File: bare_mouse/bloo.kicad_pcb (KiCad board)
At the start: 2 copper layers, 100 x 100 mm, 103 parts, among them J1 Serial Debug Header, J10 Conn_01x06_Female, J2 SWD Header, J4 Conn_ARM_JTAG_SWD_10, J5 SWD Header, M1 M1_Conn_Alt, M2 M2_Conn_Alt, Q0 TEFT4300, Q1 TEFT4300, Q10 Q_NMOS_GSD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

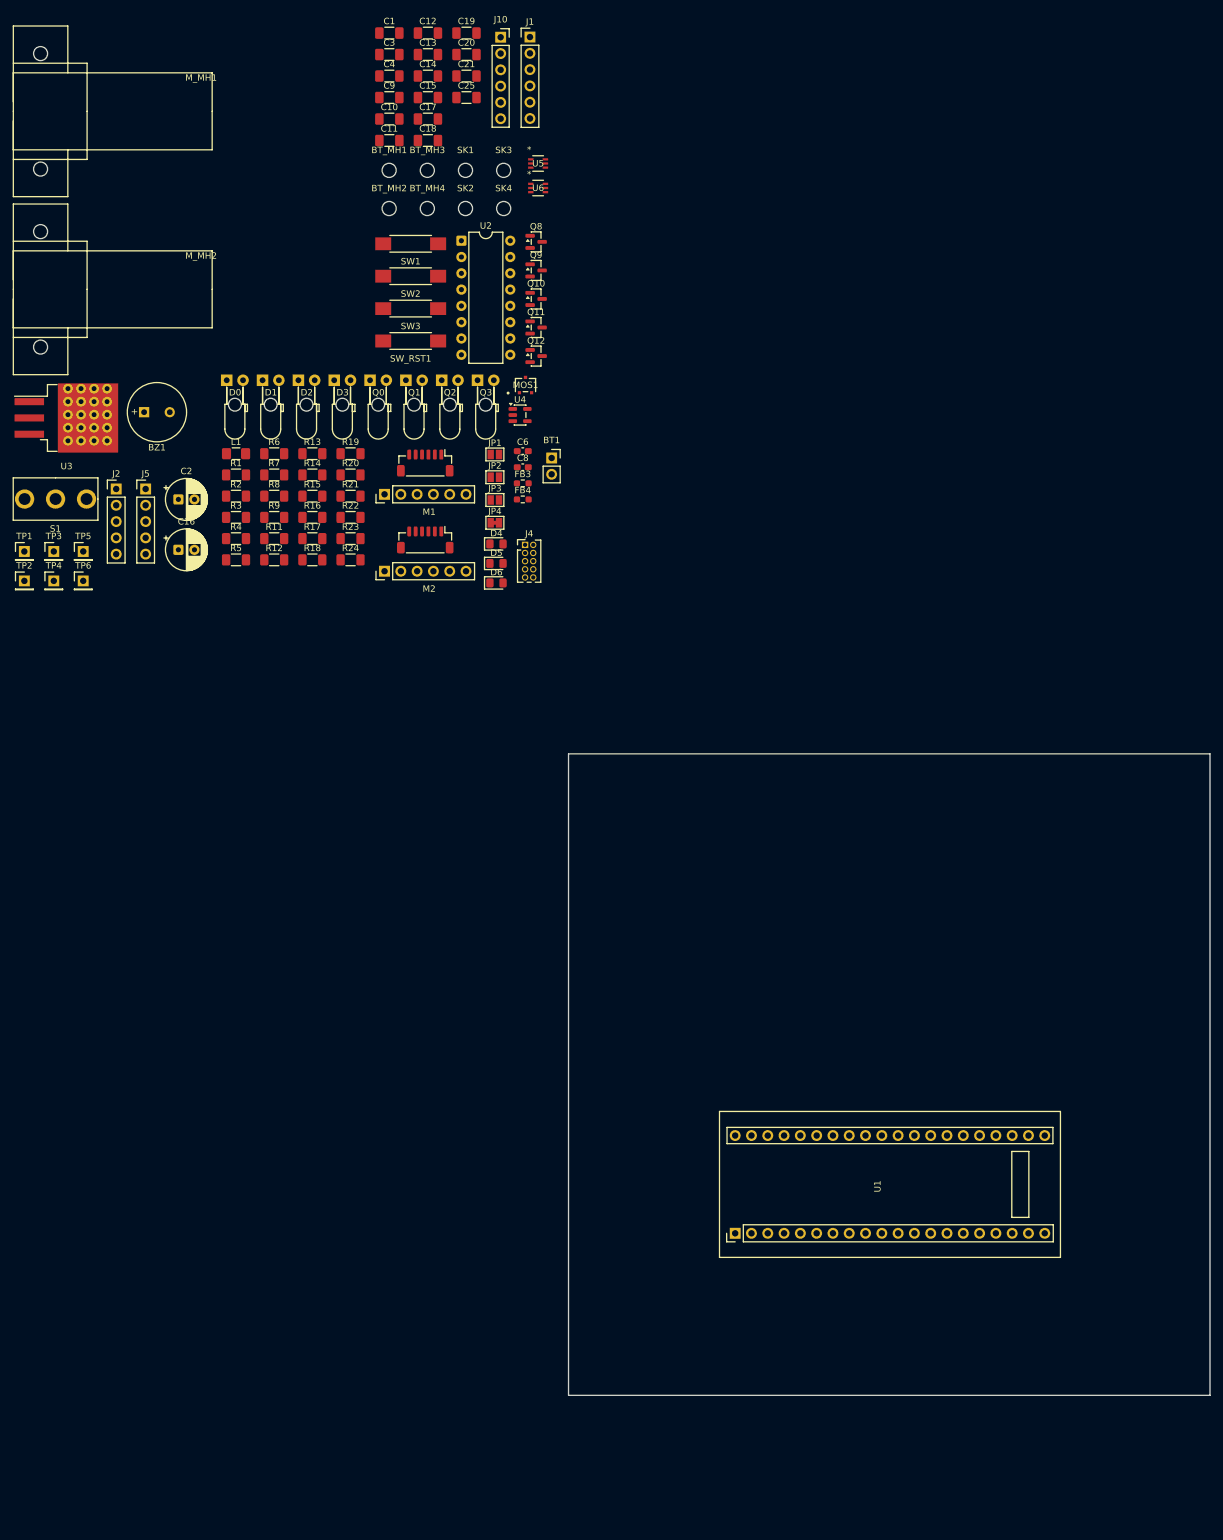
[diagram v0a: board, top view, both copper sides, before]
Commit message: [chore] include file structure for different drivers
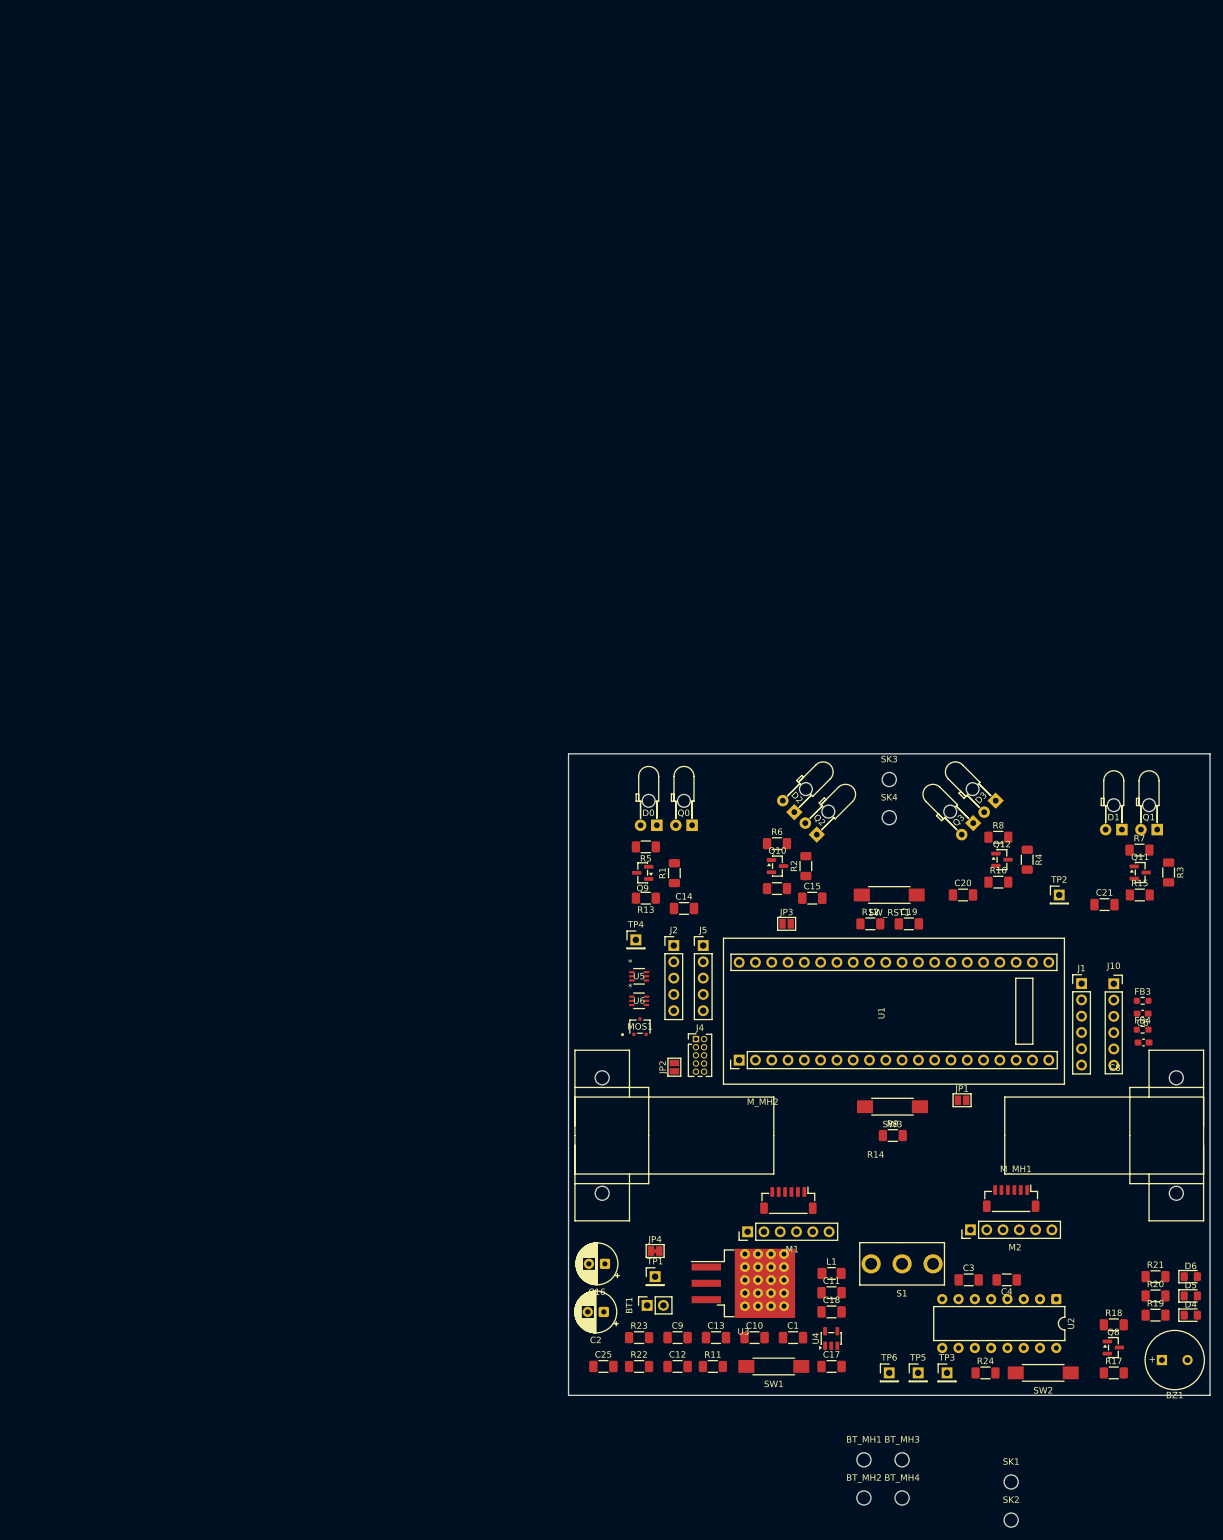
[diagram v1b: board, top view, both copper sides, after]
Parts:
- moved SK1 221.4 mm to (192.5, 248.5)
- moved SK2 221.4 mm to (192.5, 254.4)
- moved BZ1 216.8 mm to (216.0, 229.5)
- moved BT_MH1 214.2 mm to (169.6, 245.1)
- moved BT_MH3 214.2 mm to (175.5, 245.1)
- moved BT_MH2 214.2 mm to (169.6, 251.0)
- moved BT_MH4 214.2 mm to (175.5, 251.0)
- moved C1 212.9 mm to (158.5, 226.0)
- moved C12 211.5 mm to (140.5, 230.5)
- moved C3 211.3 mm to (185.9, 217.0)
- moved C4 210.9 mm to (191.8, 217.0), turned to 180 degrees
- moved C13 205.0 mm to (146.5, 226.0)
- moved C17 204.4 mm to (164.5, 230.5)
- moved M_MH1 201.9 mm to (191.5, 194.5), turned to 180 degrees
- moved C25 199.0 mm to (128.9, 230.5)
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
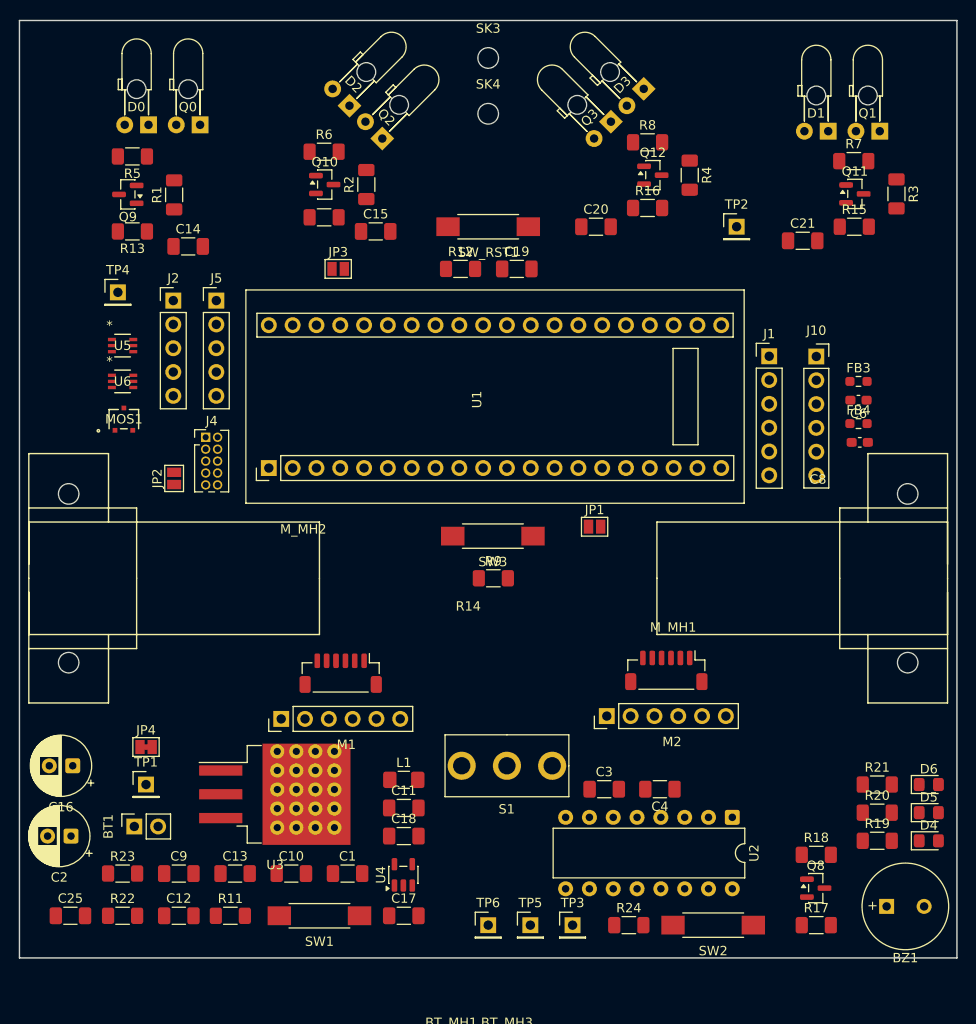
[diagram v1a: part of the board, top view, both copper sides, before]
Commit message: [feat(pid.c)] pd controller skeleton code
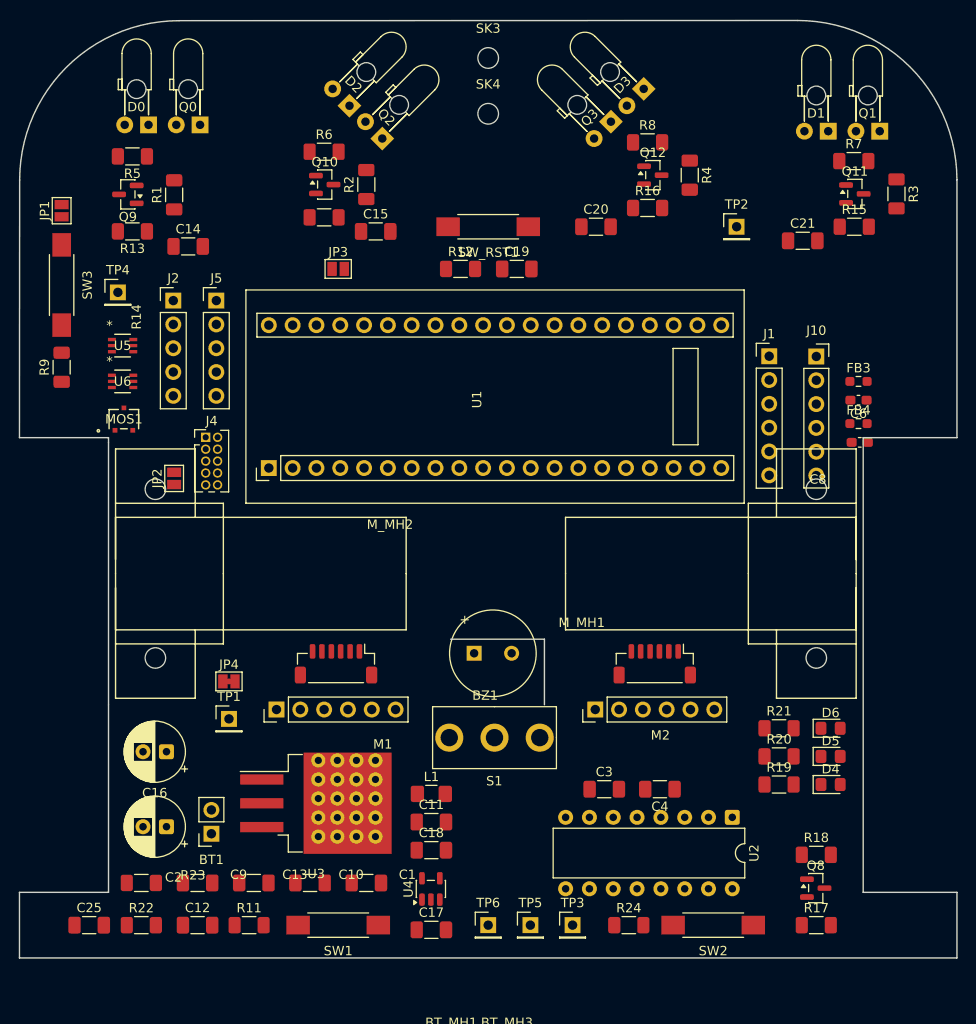
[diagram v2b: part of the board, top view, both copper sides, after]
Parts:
- moved JP1 66.1 mm to (128.0, 155.3), turned to 90 degrees
- moved SW3 53.2 mm to (128.0, 163.2), turned to 90 degrees
- moved BZ1 51.6 mm to (172.0, 202.5)
- moved R9 51.3 mm to (128.0, 172.0), turned to 90 degrees
- moved D4 12.1 mm to (210.0, 216.5)
- moved D5 12.1 mm to (210.0, 213.5)
- moved D6 12.1 mm to (210.0, 210.5)
- moved R19 12.1 mm to (204.5, 216.5)
- moved R20 12.1 mm to (204.5, 213.5)
- moved R21 12.1 mm to (204.5, 210.5)
- moved JP4 11.3 mm to (145.8, 205.5)
- moved TP1 11.3 mm to (145.8, 209.5)
- moved C2 10.2 mm to (139.2, 221.0)
- moved C16 10.1 mm to (139.2, 213.0)
- moved M_MH1 9.76 mm to (181.8, 194.0)
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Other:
- outline, holes or cut-outs redrawn
